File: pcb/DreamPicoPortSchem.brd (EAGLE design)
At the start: 30 x 75 mm, 57 parts, among them J1 FFC3B07-20-T

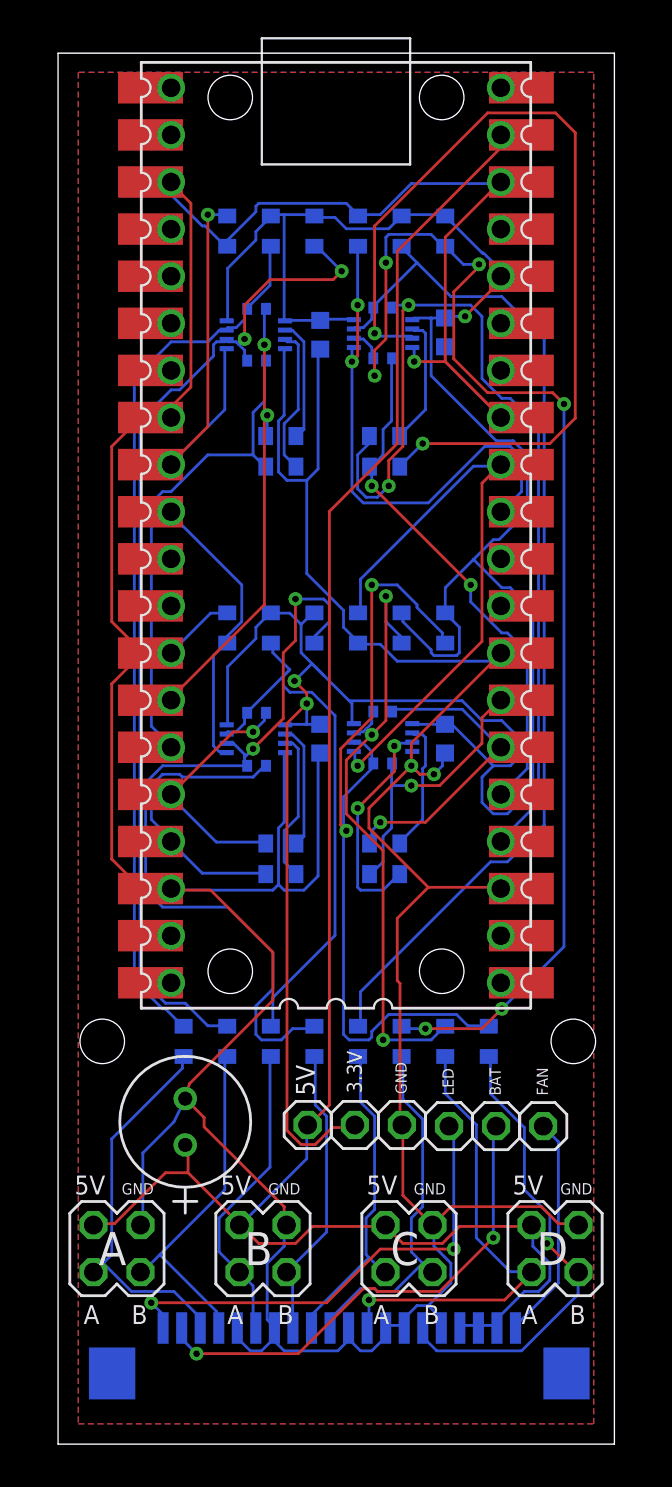
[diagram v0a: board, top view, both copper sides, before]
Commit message: 177: Uploaded Rev 1.0 board files (#180)
* 177: Uploaded Rev 1.0 board files

* 177: Changed R[A-D]1 and R[A-D]2 resistors to 1206 size

* 177: Mask vias on PCB

* 177: Added board examples

---------

Co-authored-by: James Smith <{ID}+{username}@users.noreply.github.com>
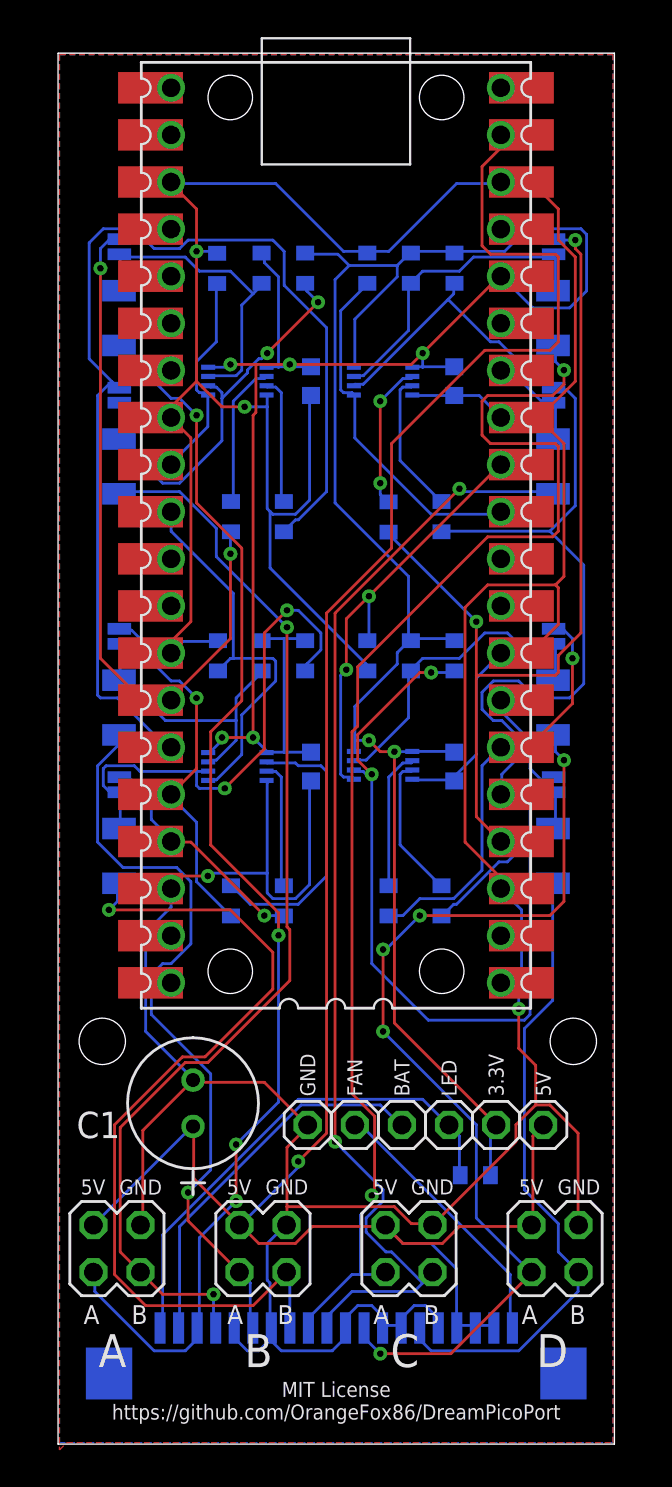
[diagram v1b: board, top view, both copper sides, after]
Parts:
- removed C5: 35ZLH100MEFC6.3X11CAP_YX_6P3X11_RUB, 2025-03-29_20-35-50_Library:CAP_YX_6P3X11_RUB
- removed R29, R30, R31, R32, R33, R34, R35, R36: NP, Jumper Pad:RESC1005X40
- added C1: 35ZLH100MEFC6.3X11CAP_YX_6P3X11_RUB, 2025-03-29_20-35-50_Library:CAP_YX_6P3X11_RUB
- added JP10, JP11, JP12, JP5, JP6, JP7, JP8, JP9: JUMPER-SMT_2_NO_NO-SILK, SparkFun-Jumpers:SMT-JUMPER_2_NO_NO-SILK
- added R8: 120, Tinkercad:RESC1608X60
- RA1, RA2, RB1, RB2, RC1, RC2, RD1, RD2: device Tinkercad:RESC1608X60 -> Resistor:RESC3216X70
- moved RC1 40.4 mm to (26.7, 60.7)
- moved RA1 39.2 mm to (3.29, 60.7)
- moved RC2 32.1 mm to (26.7, 52.7)
- moved RA2 31.5 mm to (3.29, 52.7)
- moved RB1 19.8 mm to (3.29, 39.7)
- moved RD1 18.9 mm to (26.7, 39.7)
- moved RB2 14.5 mm to (3.29, 31.7)
- moved 5V 12.7 mm to (26.2, 17.2)
- moved RD2 10.6 mm to (26.7, 31.7)
- moved FAN 10.2 mm to (16.0, 17.2)
- moved 3.3V 7.62 mm to (23.6, 17.2)
- moved RA3 5.11 mm to (9.32, 50.0), turned to 90 degrees
- moved BAT 5.08 mm to (18.5, 17.2)
- moved GND 5.08 mm to (13.5, 17.2)
- moved RC3 4.37 mm to (17.8, 50.0), turned to 270 degrees
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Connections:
- net +3.3V: now also R8.1
- net +5V: now also C1.1; no longer C5.1
- net GND: now also C1.2; no longer C5.2
- net N$11: now also JP10.1; no longer R34.2
- net N$13: now also JP8.2; no longer R32.1
- net N$15: now also JP7.2; no longer R31.1
- net N$17: now also R8.2
- net N$18: now also JP8.1; no longer R32.2
- net N$19: now also JP7.1; no longer R31.2
- net N$21: now also JP5.2; no longer R29.1
- net N$22: now also JP9.1; no longer R33.2
- net N$25: now also JP10.2; no longer R34.1
- net N$26: now also JP9.2; no longer R33.1
- net N$29: now also JP12.1; no longer R36.2
- net N$3: now also JP6.2; no longer R30.1
- net N$30: now also JP11.1; no longer R35.2
- net N$36: now also JP12.2; no longer R36.1
- net N$37: now also JP11.2; no longer R35.1
- net N$6: now also JP5.1; no longer R29.2
- net N$7: now also JP6.1; no longer R30.2
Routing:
- net C-A: track 17.8 -> 71.2 mm, vias 0 -> 2
- net N$26: track 68.8 -> 18.7 mm, vias 6 -> 0
- net A-A: track 21.4 -> 68.8 mm, vias 0 -> 4
- net C-B: track 20.4 -> 61.0 mm, vias 0 -> 2
- net A-B: track 18.9 -> 59.1 mm, vias 0 -> 2
- net N$23: track 47.7 -> 7.71 mm, vias 2 -> 0
- net N$25: track 56.9 -> 17.0 mm
- net N$21: track 27.7 -> 61.0 mm
- net N$6: track 54.8 -> 21.7 mm
- net B-B: track 15.9 -> 46.9 mm, vias 0 -> 1
- net N$7: track 48.0 -> 17.2 mm
- net D-A: track 25.2 -> 52.6 mm, vias 1 -> 5
- net B-A: track 16.6 -> 40.7 mm, vias 0 -> 1
- net N$36: track 34.5 -> 17.4 mm, vias 3 -> 0
- net N$19: track 44.3 -> 27.9 mm
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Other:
- board text added: "C1"
- board text added: "Rev 1.0"
- board text removed: "Rev 0.2"

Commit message: Updated 5V to VBUS on PCB
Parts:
- added JP13: JUMPER-SMT_2_NO_NO-SILK, SparkFun-Jumpers:SMT-JUMPER_2_NO_NO-SILK
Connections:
- removed net VBUS: U1.40, U1.P$40
- new net N$24: JP13.2, U1.39, U1.P$39
- net +5V: now also JP13.1, U1.40, U1.P$40; no longer U1.39, U1.P$39
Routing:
- net +5V: track 120.6 -> 126.4 mm
- net N$24: track 0.00 -> 3.66 mm
- net VBUS: track 1.11 -> 0.00 mm
- net +3.3V: track 162.1 -> 162.7 mm
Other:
- board text added: "Rev 1.2"
- board text removed: "Rev 1.0"

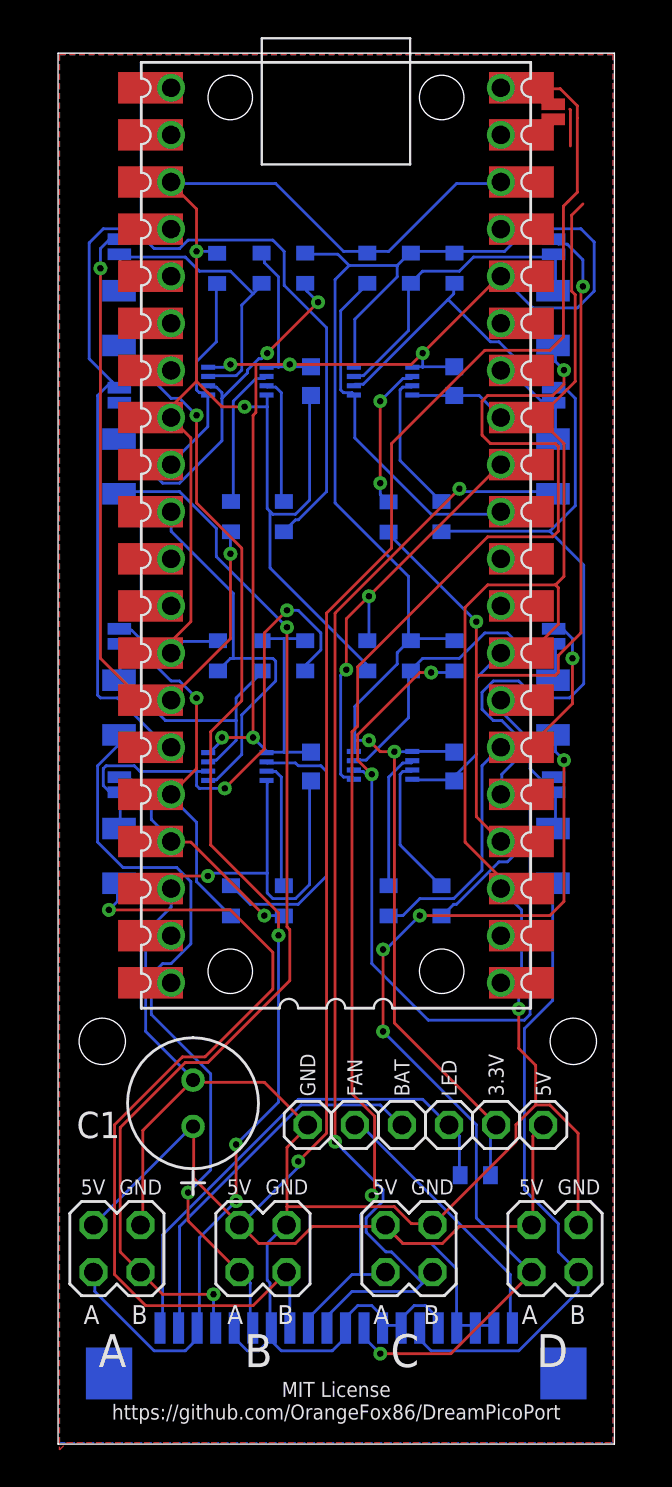
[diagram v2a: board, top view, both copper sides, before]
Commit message: Make 5V rail thicker to support 1 A max current
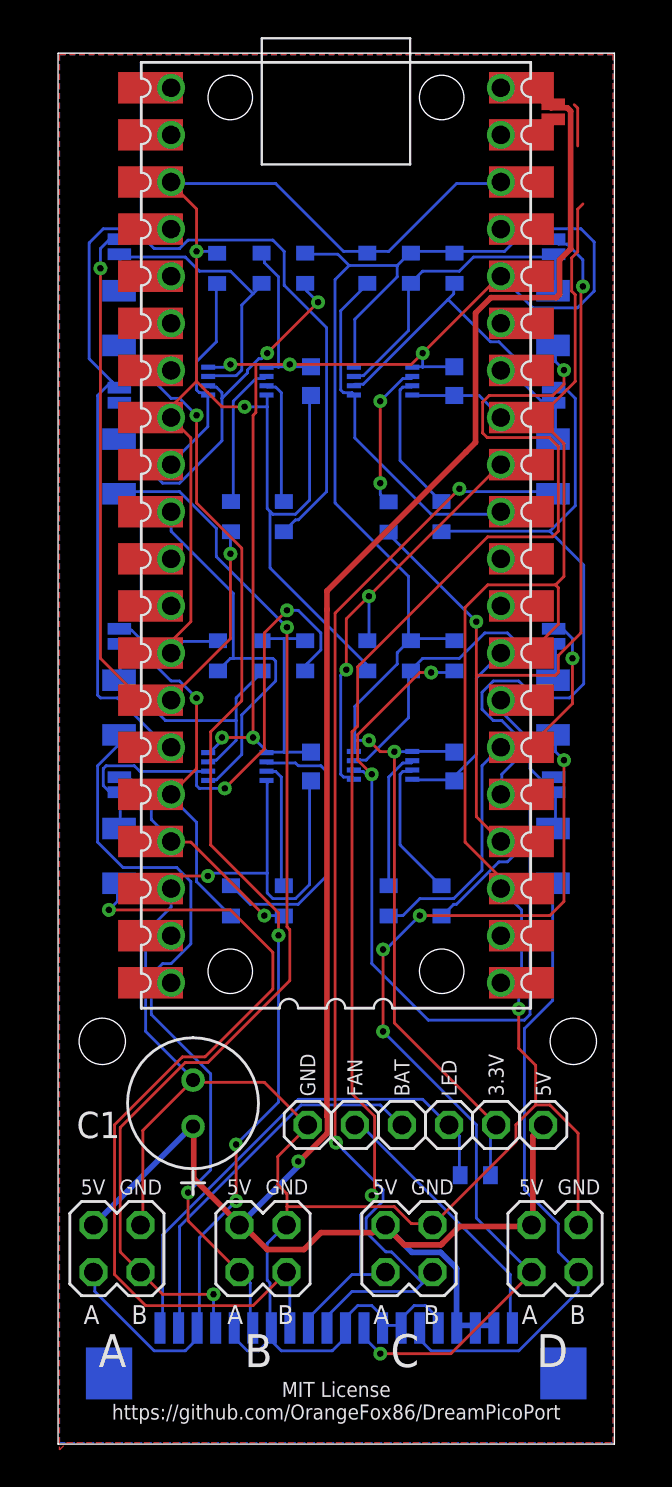
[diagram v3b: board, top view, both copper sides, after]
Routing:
- net +5V: track 126.4 -> 125.1 mm
- net GND: track 276.9 -> 277.6 mm
